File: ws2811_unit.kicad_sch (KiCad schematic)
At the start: 6 parts, among them J4 Conn_01x02, J5 Conn_01x02, J6 Conn_01x02, U3 WS2811

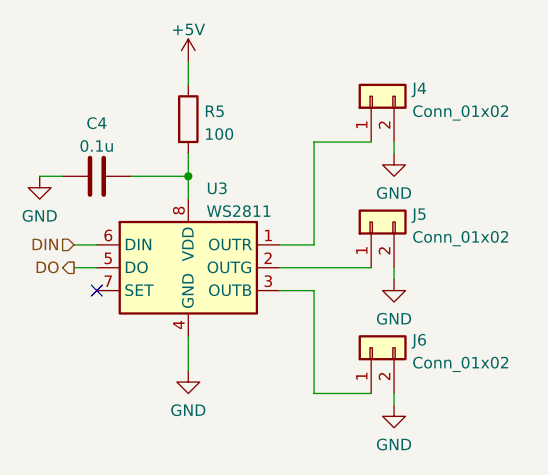
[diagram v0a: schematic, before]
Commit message: v1.1 Fix LED headers, FTDI power
Fixes from first board rev:
	- Fix LEDs to be between power and driver output
	- Change FTDI header power to 5V
	- Remove now redundant diode on FTDI power input
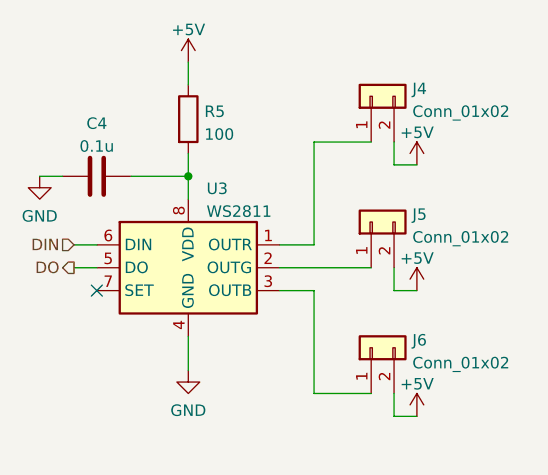
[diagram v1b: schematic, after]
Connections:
- net +5V: now also J4.2 (Pin_2), J5.2 (Pin_2), J6.2 (Pin_2)
- net GND: no longer J4.2 (Pin_2), J5.2 (Pin_2), J6.2 (Pin_2)
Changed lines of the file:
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@@
+    (stroke (width 0) (type default) (color 0 0 0 0))
+  )
+  (wire (pts (xy 157.48 93.98) (xy 157.48 96.52))
     (stroke (width 0) (type default) (color 0 0 0 0))
   )
@@
     (stroke (width 0) (type default) (color 0 0 0 0))
   )
-  (wire (pts (xy 157.48 93.98) (xy 157.48 95.25))
+  (wire (pts (xy 157.48 96.52) (xy 160.02 96.52))
     (stroke (width 0) (type default) (color 0 0 0 0))
   )
@@
     (stroke (width 0) (type default) (color 0 0 0 0))
   )
-  (wire (pts (xy 157.48 80.01) (xy 157.48 81.28))
-    (stroke (width 0) (type default) (color 0 0 0 0))
-  )
-  (wire (pts (xy 157.48 107.95) (xy 157.48 109.22))
+  (wire (pts (xy 157.48 80.01) (xy 157.48 82.55))
+    (stroke (width 0) (type default) (color 0 0 0 0))
+  )
+  (wire (pts (xy 157.48 110.49) (xy 160.02 110.49))
+    (stroke (width 0) (type default) (color 0 0 0 0))
+  )
+  (wire (pts (xy 157.48 107.95) (xy 157.48 110.49))
     (stroke (width 0) (type default) (color 0 0 0 0))
   )
   (wire (pts (xy 121.92 93.98) (xy 124.46 93.98))
+    (stroke (width 0) (type default) (color 0 0 0 0))
+  )
+  (wire (pts (xy 157.48 82.55) (xy 160.02 82.55))
     (stroke (width 0) (type default) (color 0 0 0 0))
   )
@@
     )
     (property "Datasheet" "" (id 3) (at 118.11 83.82 0)
-      (effects (font (size 1.27 1.27)) hide)
-    )
-    (pin "1")
-  )
-  (symbol (lib_id "power:GND") (at 157.48 95.25 0) (unit 1)
-    (in_bom yes) (on_board yes) (fields_autoplaced)
-    (property "Reference" "#PWR0119" (id 0) (at 157.48 101.6 0)
-      (effects (font (size 1.27 1.27)) hide)
-    )
-    (property "Value" "GND" (id 1) (at 157.48 99.6934 0))
-    (property "Footprint" "" (id 2) (at 157.48 95.25 0)
-      (effects (font (size 1.27 1.27)) hide)
-    )
-    (property "Datasheet" "" (id 3) (at 157.48 95.25 0)
       (effects (font (size 1.27 1.27)) hide)
     )
@@
     (pin "8")
   )
+  (symbol (lib_id "power:+5V") (at 160.02 110.49 0) (unit 1)
+    (in_bom yes) (on_board yes) (fields_autoplaced)
+    (property "Reference" "#PWR?" (id 0) (at 160.02 114.3 0)
+      (effects (font (size 1.27 1.27)) hide)
+    )
+    (property "Value" "+5V" (id 1) (at 160.02 106.9142 0))
+    (property "Footprint" "" (id 2) (at 160.02 110.49 0)
+      (effects (font (size 1.27 1.27)) hide)
+    )
+    (property "Datasheet" "" (id 3) (at 160.02 110.49 0)
+      (effects (font (size 1.27 1.27)) hide)
+    )
+    (pin "1")
+  )
   (symbol (lib_id "Connector_Generic:Conn_01x02") (at 154.94 88.9 90) (unit 1)
     (in_bom yes) (on_board yes) (fields_autoplaced)
@@
     )
     (property "Datasheet" "" (id 3) (at 134.62 105.41 0)
+      (effects (font (size 1.27 1.27)) hide)
+    )
+    (pin "1")
+  )
+  (symbol (lib_id "power:+5V") (at 160.02 82.55 0) (unit 1)
+    (in_bom yes) (on_board yes) (fields_autoplaced)
+    (property "Reference" "#PWR?" (id 0) (at 160.02 86.36 0)
+      (effects (font (size 1.27 1.27)) hide)
+    )
+    (property "Value" "+5V" (id 1) (at 160.02 78.9742 0))
+    (property "Footprint" "" (id 2) (at 160.02 82.55 0)
+      (effects (font (size 1.27 1.27)) hide)
+    )
+    (property "Datasheet" "" (id 3) (at 160.02 82.55 0)
       (effects (font (size 1.27 1.27)) hide)
     )
@@
     (pin "2")
   )
-  (symbol (lib_id "power:GND") (at 157.48 109.22 0) (unit 1)
-    (in_bom yes) (on_board yes) (fields_autoplaced)
-    (property "Reference" "#PWR0120" (id 0) (at 157.48 115.57 0)
-      (effects (font (size 1.27 1.27)) hide)
-    )
-    (property "Value" "GND" (id 1) (at 157.48 113.6634 0))
-    (property "Footprint" "" (id 2) (at 157.48 109.22 0)
-      (effects (font (size 1.27 1.27)) hide)
-    )
-    (property "Datasheet" "" (id 3) (at 157.48 109.22 0)
-      (effects (font (size 1.27 1.27)) hide)
-    )
-    (pin "1")
-  )
   (symbol (lib_id "power:+5V") (at 134.62 71.12 0) (unit 1)
     (in_bom yes) (on_board yes) (fields_autoplaced)
@@
     (pin "1")
   )
+  (symbol (lib_id "power:+5V") (at 160.02 96.52 0) (unit 1)
+    (in_bom yes) (on_board yes) (fields_autoplaced)
+    (property "Reference" "#PWR?" (id 0) (at 160.02 100.33 0)
+      (effects (font (size 1.27 1.27)) hide)
+    )
+    (property "Value" "+5V" (id 1) (at 160.02 92.9442 0))
+    (property "Footprint" "" (id 2) (at 160.02 96.52 0)
+      (effects (font (size 1.27 1.27)) hide)
+    )
+    (property "Datasheet" "" (id 3) (at 160.02 96.52 0)
+      (effects (font (size 1.27 1.27)) hide)
+    )
+    (pin "1")
+  )
   (symbol (lib_id "Device:R") (at 134.62 77.47 0) (unit 1)
     (in_bom yes) (on_board yes) (fields_autoplaced)
@@
     (pin "2")
   )
-  (symbol (lib_id "power:GND") (at 157.48 81.28 0) (unit 1)
-    (in_bom yes) (on_board yes) (fields_autoplaced)
-    (property "Reference" "#PWR0118" (id 0) (at 157.48 87.63 0)
-      (effects (font (size 1.27 1.27)) hide)
-    )
-    (property "Value" "GND" (id 1) (at 157.48 85.7234 0))
-    (property "Footprint" "" (id 2) (at 157.48 81.28 0)
-      (effects (font (size 1.27 1.27)) hide)
-    )
-    (property "Datasheet" "" (id 3) (at 157.48 81.28 0)
-      (effects (font (size 1.27 1.27)) hide)
-    )
-    (pin "1")
-  )
   (symbol (lib_id "Connector_Generic:Conn_01x02") (at 154.94 74.93 90) (unit 1)
